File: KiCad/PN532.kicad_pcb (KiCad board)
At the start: 2 copper layers, 42 x 42 mm, 41 parts, among them J1 Header, J2 SPOX, J3 MiniGrid, SW1 TAMPER, U1 PN532, Y1 27.12MHz (Mouser 830053099)

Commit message: Tweak
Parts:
- added AJK1: AJK, RevK:AJK-Silk, B.Cu at (136.7, 77.1)
- moved J1 0.21 mm to (117.2, 87.0)
- moved J2 0.15 mm to (117.2, 88.4)
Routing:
- net +5V: track 35.2 -> 37.6 mm
- net Net-(J1-Pad4): track 31.5 -> 33.7 mm

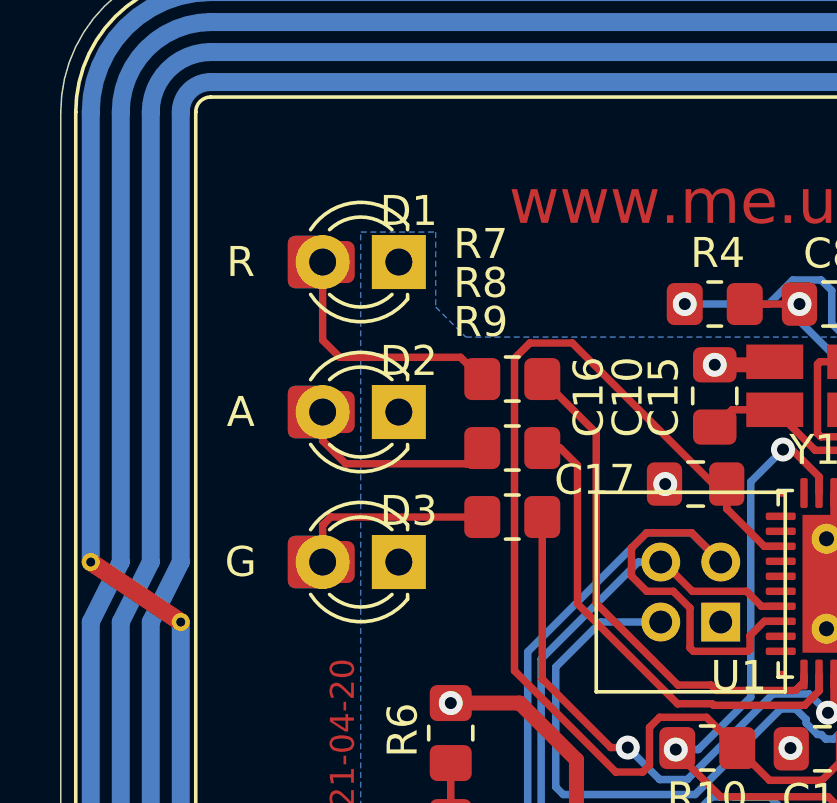
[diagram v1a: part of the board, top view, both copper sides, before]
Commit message: Position LEDs neater
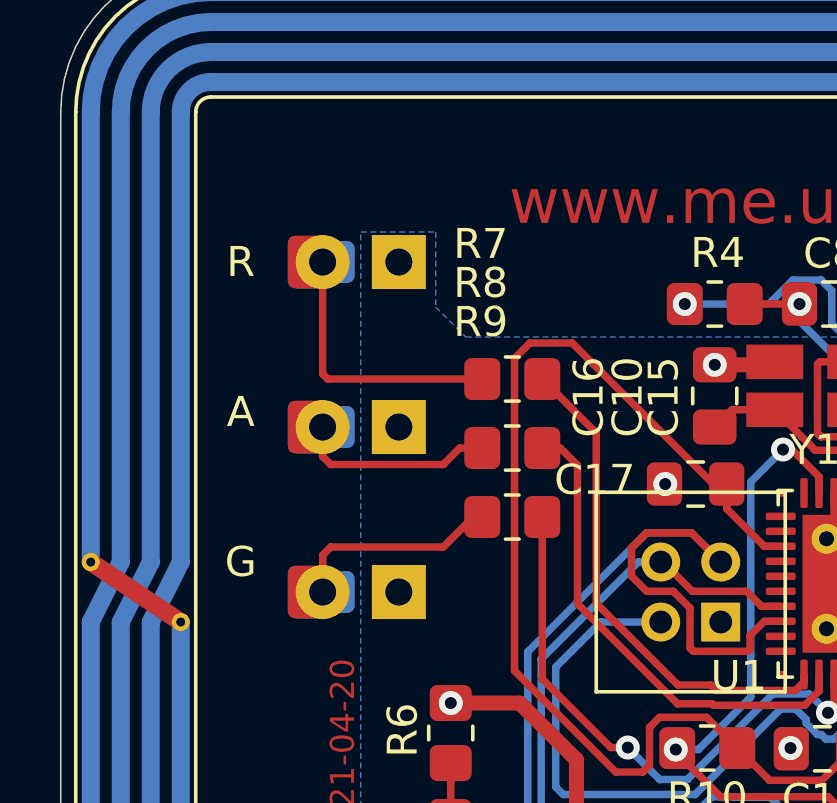
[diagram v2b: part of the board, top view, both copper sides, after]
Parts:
- D1, D2, D3: moved to B.Cu
- moved D3 1.00 mm to (110.0, 79.0)
- moved D2 0.50 mm to (110.0, 73.5)
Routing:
- net Net-(D2-Pad2): track 6.81 -> 7.59 mm
- net Net-(D1-Pad2): track 8.46 -> 9.12 mm
